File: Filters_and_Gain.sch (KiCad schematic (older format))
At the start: 20 parts, among them U4 OPA388, U5 OPA388, U6 OPA388

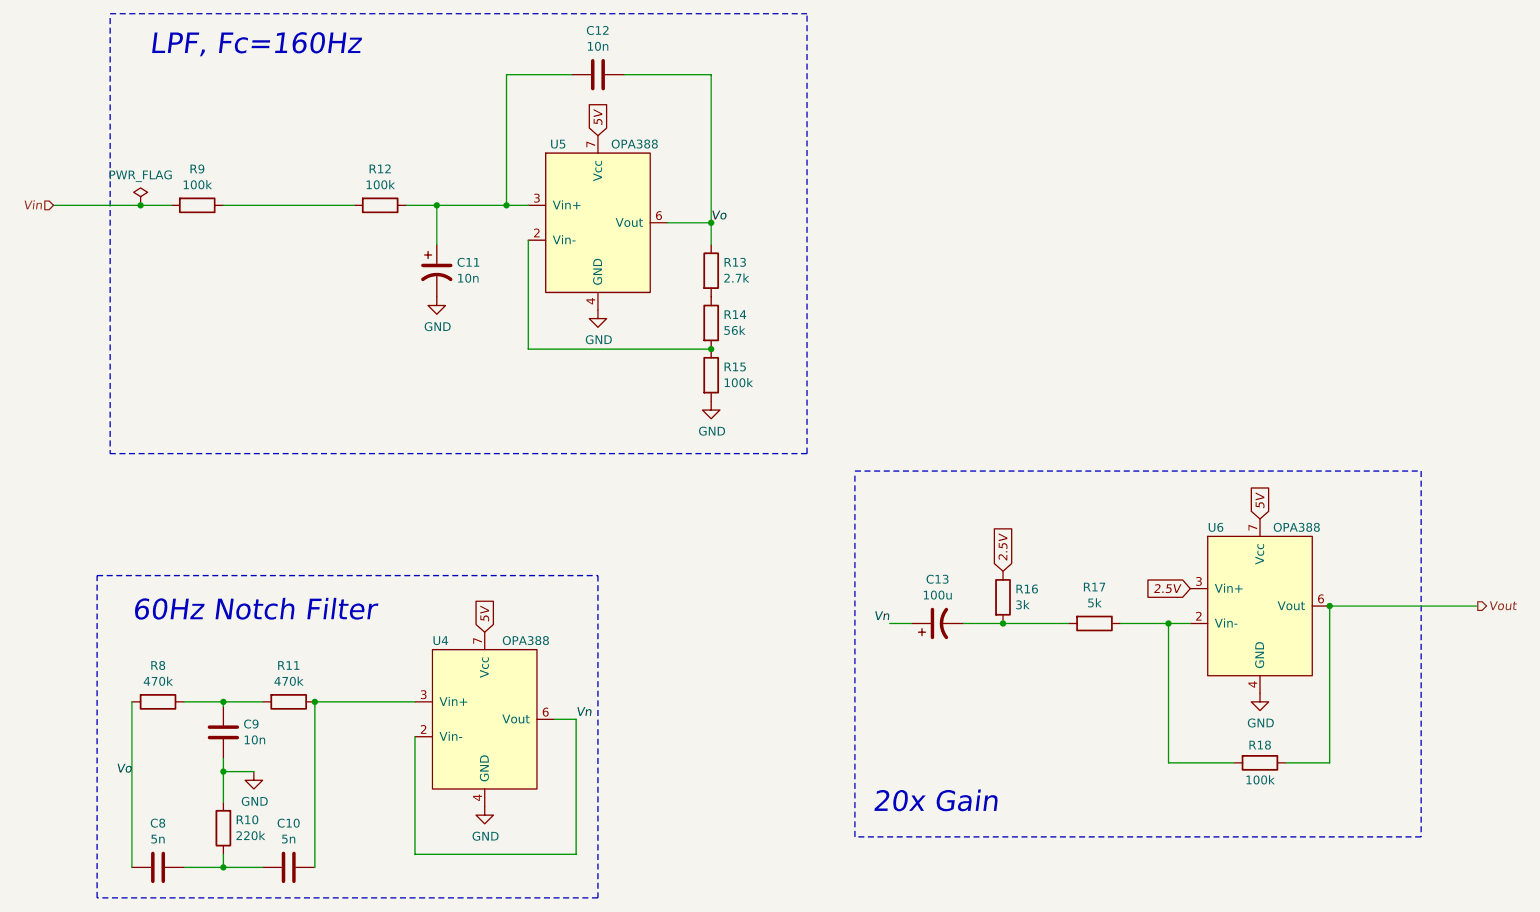
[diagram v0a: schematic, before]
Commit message: #8 - Add test points. (Also updated filter circuit)
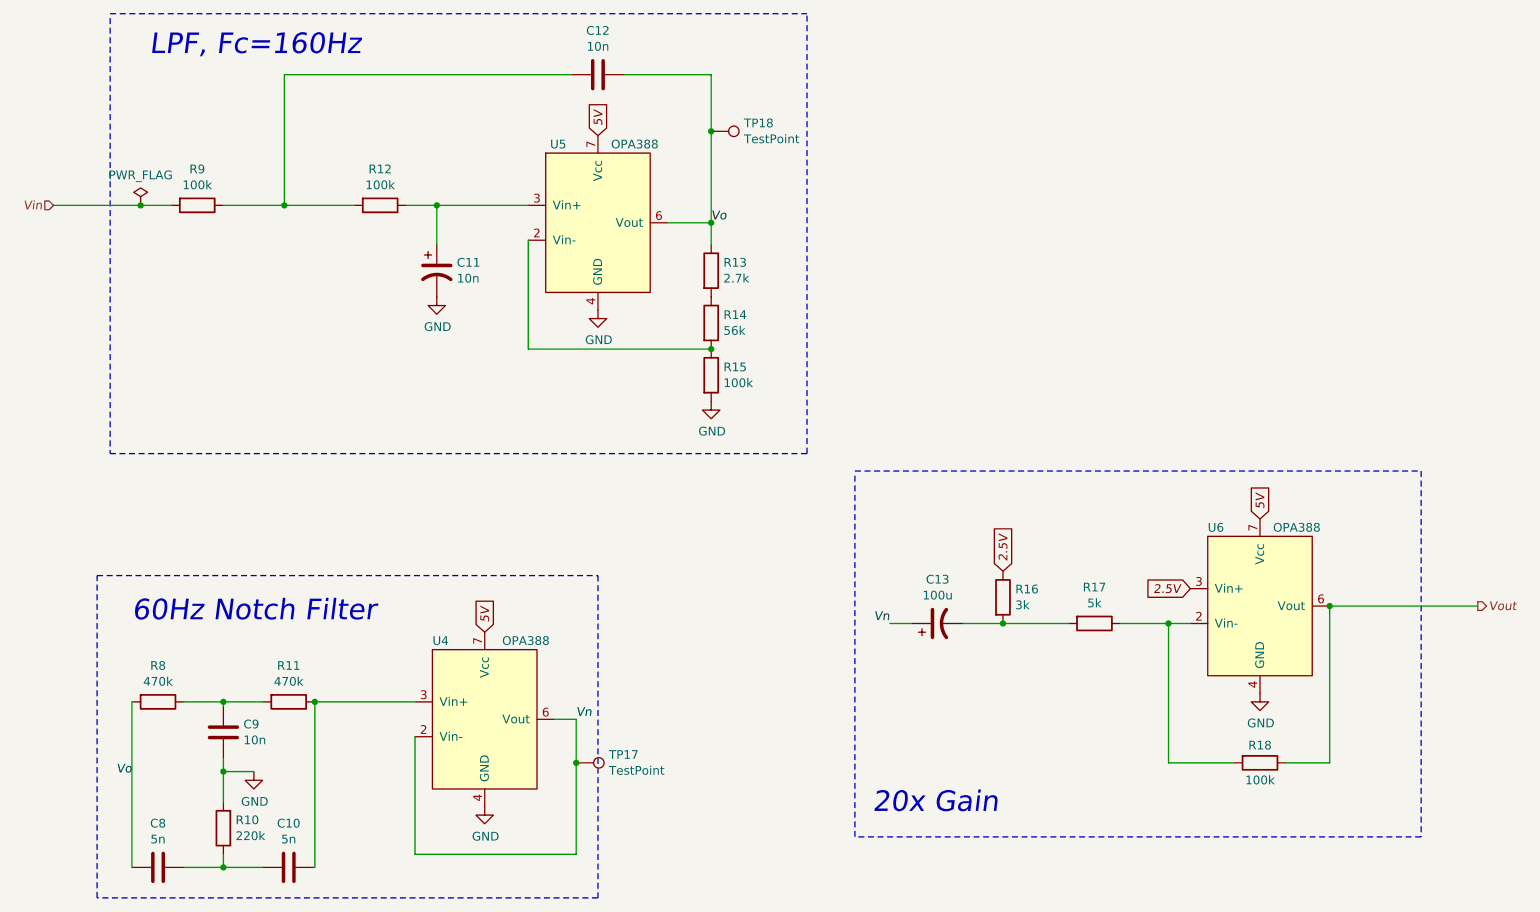
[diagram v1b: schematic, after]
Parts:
- added TP17, TP18: TestPoint, TestPoint:TestPoint_Pad_D2.0mm, symbol Connector:TestPoint
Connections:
- net Vn: now also TP17.1
- net Vo: now also TP18.1
- net at R12.2, R9.1: now also C12.1
- net at C11.1, R12.1, U5.3 (Vin+): no longer C12.1
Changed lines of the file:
@@
 $EndComp
 Wire Wire Line
-	2825 2200 3575 2200
+	2825 2200 3175 2200
 $Comp
 L Device:CP1 C11
@@
 	1    0    0    -1
 $EndComp
-Wire Wire Line
-	4575 2200 4450 2200
 Connection ~ 4050 2200
 $Comp
@@
 	1    0    0    -1
 $EndComp
-Connection ~ 4450 2200
-Wire Wire Line
-	4450 2200 4050 2200
 $Comp
 L power:GND #PWR08
@@
 5V
 Wire Wire Line
-	4825 1450 4450 1450
-Wire Wire Line
-	4450 1450 4450 2200
-Wire Wire Line
 	5125 1450 5625 1450
 Wire Wire Line
@@
 Connection ~ 5625 3025
 Wire Wire Line
-	5625 1450 5625 2300
+	5625 1450 5625 1775
 Wire Wire Line
 	5625 2300 5625 2425
@@
 	3925 5925 4850 5925
 Wire Wire Line
-	4850 5925 4850 5150
+	4850 5925 4850 5400
 Wire Wire Line
 	4850 5150 4725 5150
@@
 	2350 2200 2525 2200
 Connection ~ 2350 2200
+Wire Wire Line
+	4050 2200 4575 2200
+Wire Wire Line
+	3175 1450 3175 2200
+Wire Wire Line
+	3175 1450 4825 1450
+Connection ~ 3175 2200
+Wire Wire Line
+	3175 2200 3575 2200
+$Comp
+L Connector:TestPoint TP18
+U 1 1 5FCA32EA
+P 5625 1775
+F 0 "TP18" V 5579 1963 50  0000 L CNN
+F 1 "TestPoint" V 5670 1963 50  0000 L CNN
+F 2 "TestPoint:TestPoint_Pad_D2.0mm" H 5825 1775 50  0001 C CNN
+F 3 "~" H 5825 1775 50  0001 C CNN
+	1    5625 1775
+	0    1    1    0
+$EndComp
+Connection ~ 5625 1775
+Wire Wire Line
+	5625 1775 5625 2300
+$Comp
+L Connector:TestPoint TP17
+U 1 1 5FCA48ED
+P 4850 5400
+F 0 "TP17" V 4804 5588 50  0000 L CNN
+F 1 "TestPoint" V 4895 5588 50  0000 L CNN
+F 2 "TestPoint:TestPoint_Pad_D2.0mm" H 5050 5400 50  0001 C CNN
+F 3 "~" H 5050 5400 50  0001 C CNN
+	1    4850 5400
+	0    1    1    0
+$EndComp
+Connection ~ 4850 5400
+Wire Wire Line
+	4850 5400 4850 5150
 $EndSCHEMATC

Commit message: #4 - Added the heart edge cut and updated the Kicad footprints that were removed
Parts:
- C10, C11, C12, C8, C9: footprint Capacitor_SMD:C_0805_2012Metric_Pad1.15x1.40mm_HandSolder -> Capacitor_SMD:C_0805_2012Metric_Pad1.18x1.45mm_HandSolder
- R10, R11, R12, R13, R14, R15, R16, R17, R18, R8, R9: footprint Resistor_SMD:R_0805_2012Metric_Pad1.15x1.40mm_HandSolder -> Resistor_SMD:R_0805_2012Metric_Pad1.20x1.40mm_HandSolder
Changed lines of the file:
@@
 F 0 "R9" V 2468 2200 50  0000 C CNN
 F 1 "100k" V 2559 2200 50  0000 C CNN
-F 2 "Resistor_SMD:R_0805_2012Metric_Pad1.15x1.40mm_HandSolder" V 2605 2200 50  0001 C CNN
+F 2 "Resistor_SMD:R_0805_2012Metric_Pad1.20x1.40mm_HandSolder" V 2605 2200 50  0001 C CNN
 F 3 "~" H 2675 2200 50  0001 C CNN
 	1    2675 2200
@@
 F 0 "R12" V 3518 2200 50  0000 C CNN
 F 1 "100k" V 3609 2200 50  0000 C CNN
-F 2 "Resistor_SMD:R_0805_2012Metric_Pad1.15x1.40mm_HandSolder" V 3655 2200 50  0001 C CNN
+F 2 "Resistor_SMD:R_0805_2012Metric_Pad1.20x1.40mm_HandSolder" V 3655 2200 50  0001 C CNN
 F 3 "~" H 3725 2200 50  0001 C CNN
 	1    3725 2200
@@
 F 0 "C11" H 4165 2621 50  0000 L CNN
 F 1 "10n" H 4165 2530 50  0000 L CNN
-F 2 "Capacitor_SMD:C_0805_2012Metric_Pad1.15x1.40mm_HandSolder" H 4050 2575 50  0001 C CNN
+F 2 "Capacitor_SMD:C_0805_2012Metric_Pad1.18x1.45mm_HandSolder" H 4050 2575 50  0001 C CNN
 F 3 "~" H 4050 2575 50  0001 C CNN
 	1    4050 2575
@@
 F 0 "R15" H 5695 3221 50  0000 L CNN
 F 1 "100k" H 5695 3130 50  0000 L CNN
-F 2 "Resistor_SMD:R_0805_2012Metric_Pad1.15x1.40mm_HandSolder" V 5555 3175 50  0001 C CNN
+F 2 "Resistor_SMD:R_0805_2012Metric_Pad1.20x1.40mm_HandSolder" V 5555 3175 50  0001 C CNN
 F 3 "~" H 5625 3175 50  0001 C CNN
 	1    5625 3175
@@
 F 0 "C12" V 5227 1450 50  0000 C CNN
 F 1 "10n" V 5136 1450 50  0000 C CNN
-F 2 "Capacitor_SMD:C_0805_2012Metric_Pad1.15x1.40mm_HandSolder" H 5013 1300 50  0001 C CNN
+F 2 "Capacitor_SMD:C_0805_2012Metric_Pad1.18x1.45mm_HandSolder" H 5013 1300 50  0001 C CNN
 F 3 "~" H 4975 1450 50  0001 C CNN
 	1    4975 1450
@@
 F 0 "R14" H 5695 2921 50  0000 L CNN
 F 1 "56k" H 5695 2830 50  0000 L CNN
-F 2 "Resistor_SMD:R_0805_2012Metric_Pad1.15x1.40mm_HandSolder" V 5555 2875 50  0001 C CNN
+F 2 "Resistor_SMD:R_0805_2012Metric_Pad1.20x1.40mm_HandSolder" V 5555 2875 50  0001 C CNN
 F 3 "~" H 5625 2875 50  0001 C CNN
 	1    5625 2875
@@
 F 0 "R13" H 5695 2621 50  0000 L CNN
 F 1 "2.7k" H 5695 2530 50  0000 L CNN
-F 2 "Resistor_SMD:R_0805_2012Metric_Pad1.15x1.40mm_HandSolder" V 5555 2575 50  0001 C CNN
+F 2 "Resistor_SMD:R_0805_2012Metric_Pad1.20x1.40mm_HandSolder" V 5555 2575 50  0001 C CNN
 F 3 "~" H 5625 2575 50  0001 C CNN
 	1    5625 2575
@@
 F 0 "R8" V 2243 5050 50  0000 C CNN
 F 1 "470k" V 2334 5050 50  0000 C CNN
-F 2 "Resistor_SMD:R_0805_2012Metric_Pad1.15x1.40mm_HandSolder" V 2380 5050 50  0001 C CNN
+F 2 "Resistor_SMD:R_0805_2012Metric_Pad1.20x1.40mm_HandSolder" V 2380 5050 50  0001 C CNN
 F 3 "~" H 2450 5050 50  0001 C CNN
 	1    2450 5050
@@
 F 0 "R11" V 2993 5050 50  0000 C CNN
 F 1 "470k" V 3084 5050 50  0000 C CNN
-F 2 "Resistor_SMD:R_0805_2012Metric_Pad1.15x1.40mm_HandSolder" V 3130 5050 50  0001 C CNN
+F 2 "Resistor_SMD:R_0805_2012Metric_Pad1.20x1.40mm_HandSolder" V 3130 5050 50  0001 C CNN
 F 3 "~" H 3200 5050 50  0001 C CNN
 	1    3200 5050
@@
 F 0 "R10" H 2755 5729 50  0000 R CNN
 F 1 "220k" H 2755 5820 50  0000 R CNN
-F 2 "Resistor_SMD:R_0805_2012Metric_Pad1.15x1.40mm_HandSolder" V 2755 5775 50  0001 C CNN
+F 2 "Resistor_SMD:R_0805_2012Metric_Pad1.20x1.40mm_HandSolder" V 2755 5775 50  0001 C CNN
 F 3 "~" H 2825 5775 50  0001 C CNN
 	1    2825 5775
@@
 F 0 "C8" V 2198 6000 50  0000 C CNN
 F 1 "5n" V 2289 6000 50  0000 C CNN
-F 2 "Capacitor_SMD:C_0805_2012Metric_Pad1.15x1.40mm_HandSolder" H 2488 5850 50  0001 C CNN
+F 2 "Capacitor_SMD:C_0805_2012Metric_Pad1.18x1.45mm_HandSolder" H 2488 5850 50  0001 C CNN
 F 3 "~" H 2450 6000 50  0001 C CNN
 	1    2450 6000
@@
 F 0 "C10" V 2948 6000 50  0000 C CNN
 F 1 "5n" V 3039 6000 50  0000 C CNN
-F 2 "Capacitor_SMD:C_0805_2012Metric_Pad1.15x1.40mm_HandSolder" H 3238 5850 50  0001 C CNN
+F 2 "Capacitor_SMD:C_0805_2012Metric_Pad1.18x1.45mm_HandSolder" H 3238 5850 50  0001 C CNN
 F 3 "~" H 3200 6000 50  0001 C CNN
 	1    3200 6000
@@
 F 0 "C9" H 2710 5179 50  0000 R CNN
 F 1 "10n" H 2710 5270 50  0000 R CNN
-F 2 "Capacitor_SMD:C_0805_2012Metric_Pad1.15x1.40mm_HandSolder" H 2863 5075 50  0001 C CNN
+F 2 "Capacitor_SMD:C_0805_2012Metric_Pad1.18x1.45mm_HandSolder" H 2863 5075 50  0001 C CNN
 F 3 "~" H 2825 5225 50  0001 C CNN
 	1    2825 5225
@@
 F 0 "R16" H 7370 4496 50  0000 L CNN
 F 1 "3k" H 7370 4405 50  0000 L CNN
-F 2 "Resistor_SMD:R_0805_2012Metric_Pad1.15x1.40mm_HandSolder" V 7230 4450 50  0001 C CNN
+F 2 "Resistor_SMD:R_0805_2012Metric_Pad1.20x1.40mm_HandSolder" V 7230 4450 50  0001 C CNN
 F 3 "~" H 7300 4450 50  0001 C CNN
 	1    7300 4450
@@
 F 0 "R17" V 7618 4600 50  0000 C CNN
 F 1 "5k" V 7709 4600 50  0000 C CNN
-F 2 "Resistor_SMD:R_0805_2012Metric_Pad1.15x1.40mm_HandSolder" V 7755 4600 50  0001 C CNN
+F 2 "Resistor_SMD:R_0805_2012Metric_Pad1.20x1.40mm_HandSolder" V 7755 4600 50  0001 C CNN
 F 3 "~" H 7825 4600 50  0001 C CNN
 	1    7825 4600
@@
 F 0 "R18" V 8675 5400 50  0000 C CNN
 F 1 "100k" V 8875 5400 50  0000 C CNN
-F 2 "Resistor_SMD:R_0805_2012Metric_Pad1.15x1.40mm_HandSolder" V 8705 5400 50  0001 C CNN
+F 2 "Resistor_SMD:R_0805_2012Metric_Pad1.20x1.40mm_HandSolder" V 8705 5400 50  0001 C CNN
 F 3 "~" H 8775 5400 50  0001 C CNN
 	1    8775 5400
